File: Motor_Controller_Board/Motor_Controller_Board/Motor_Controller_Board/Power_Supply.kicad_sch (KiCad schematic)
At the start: 11 parts, among them J201 Conn_01x02, J202 Conn_01x02, U201 TP6841S6

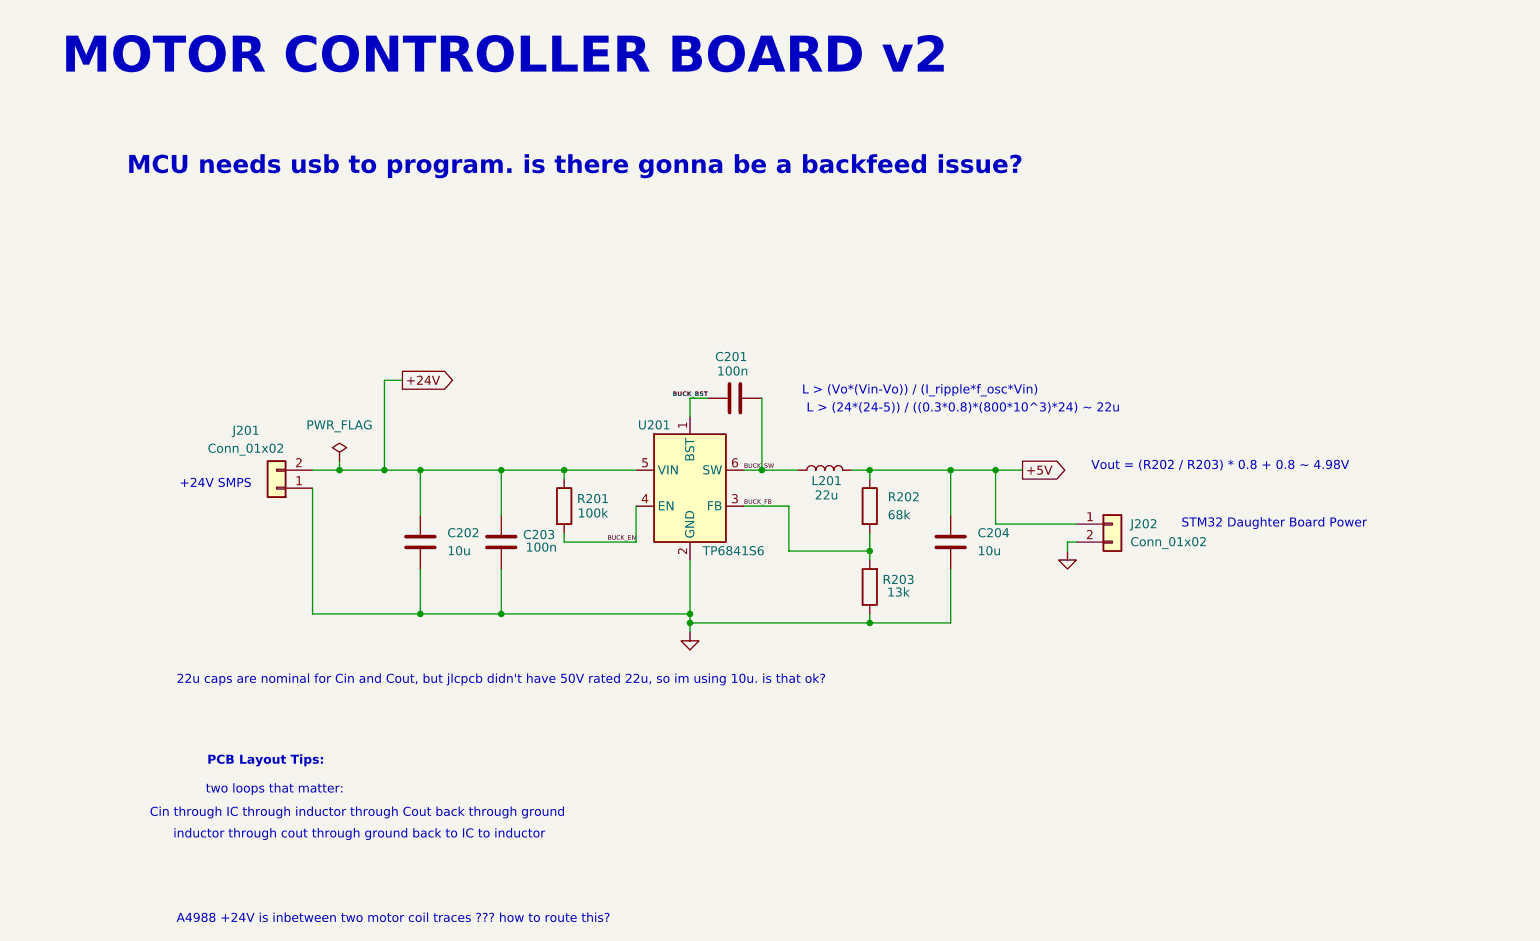
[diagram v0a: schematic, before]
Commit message: discussed with Alex and Mishari. confident in schematic, going to do layout tomorrow
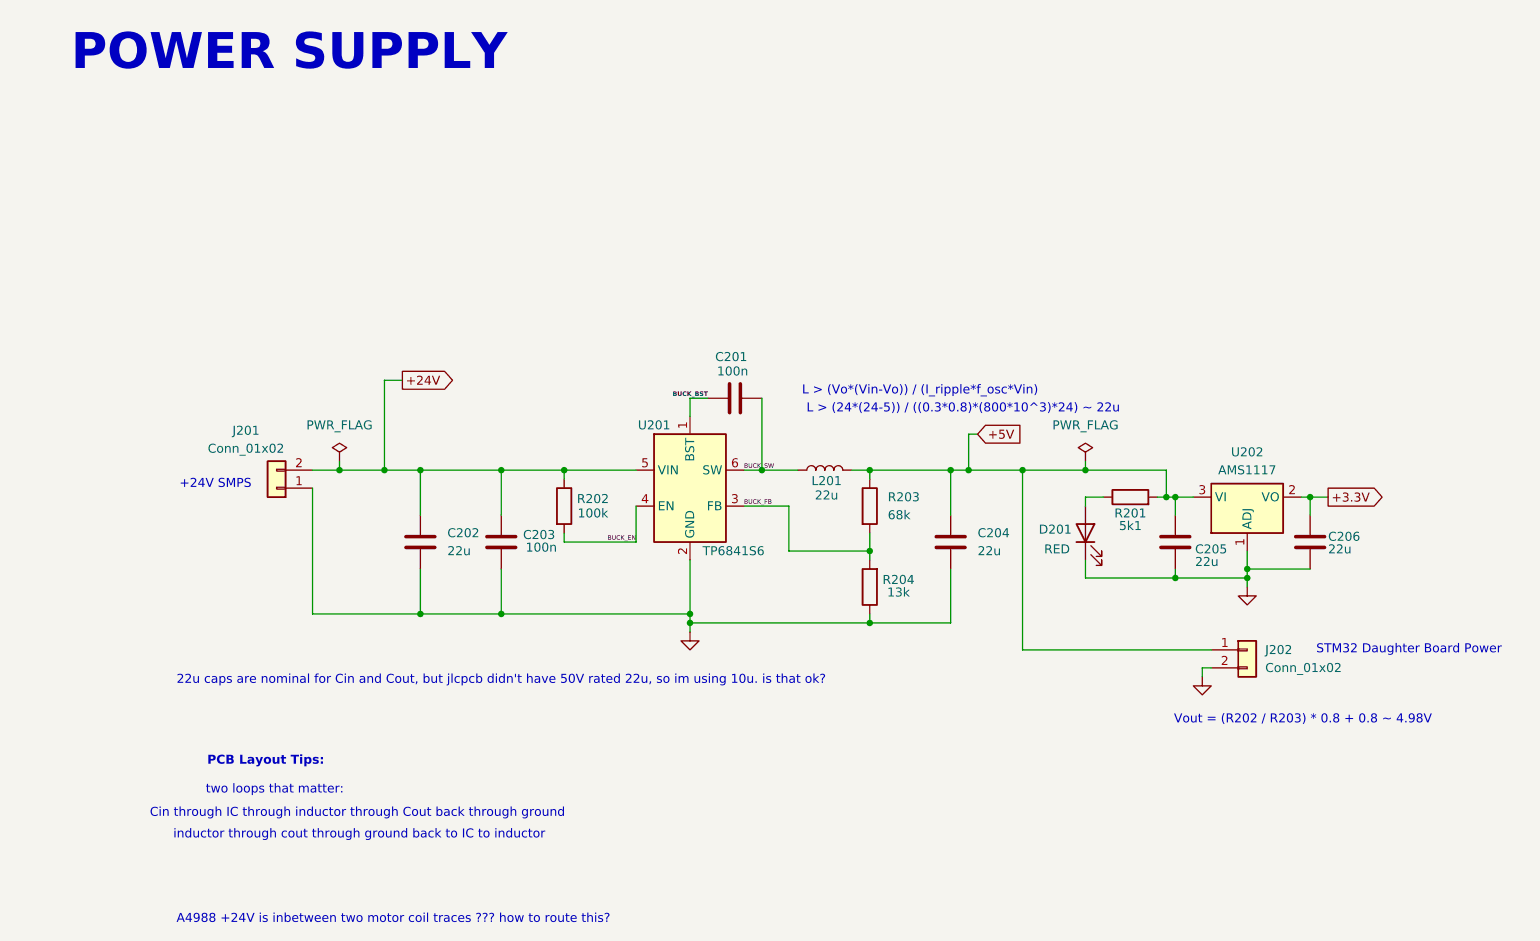
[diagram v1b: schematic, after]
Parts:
- added C205, C206: 22u, Capacitor_SMD:C_0603_1608Metric, symbol Device:C
- added D201: RED, LED_SMD:LED_0603_1608Metric, symbol Device:LED
- added R201: 5k1, Resistor_SMD:R_0603_1608Metric, symbol Device:R
- added U202: AMS1117, Package_TO_SOT_SMD:SOT-223-3_TabPin2, symbol Regulator_Linear:AMS1117
- C202, C204: value 10u -> 22u; footprint Capacitor_SMD:C_0805_2012Metric -> Capacitor_SMD:C_2220_5750Metric; LCSC Part Number C440198 -> C784103; MPN GRM21BR61H106KE43L -> FS55X226K500EHG; Manufacturer Murata Electronics -> PSA(Prosperity Dielectrics)
- J202: now left out of the parts list
- renumbered R201 to R202, R202 to R203, R203 to R204
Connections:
- net +5V: now also C205.1, R201.2, U202.3 (VI)
- net GND: now also C205.2, C206.2, D201.1 (K), U202.1 (ADJ)
- new net: D201.2 (A), R201.1
- new net +3.3V: C206.1, U202.2 (VO)
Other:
- note added: "POWER SUPPLY"
- note removed: "MCU needs usb to program. is there gonna be a backfeed issue?"
- note removed: "MOTOR CONTROLLER BOARD v2"
- moved on the sheet: J202

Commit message: routing 75% finished, but very sloppy
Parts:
- added J203: Conn_01x02, TerminalBlock:TerminalBlock_bornier-2_P5.08mm, symbol Connector_Generic:Conn_01x02
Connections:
- net +24V: now also J203.2 (Pin_2); no longer C202.1, C203.2, J201.2 (Pin_2), R202.1, U201.5 (VIN)
- net GND: now also J203.1 (Pin_1)
- new net DIGITAL_POWER_+24V: C202.1, C203.2, J201.2 (Pin_2), R202.1, U201.5 (VIN)
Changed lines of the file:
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@@
+		)
+	)
+	(text "+24V SMPS"
+		(exclude_from_sim no)
+		(at 32.004 54.102 0)
+		(effects
+			(font
+				(size 1.27 1.27)
+			)
 		)
 	)
@@
 	)
 	(junction
-		(at 55.88 76.2)
-		(diameter 0)
-		(color 0 0 0 0)
-	)
-	(junction
 		(at 167.64 91.44)
 		(diameter 0)
@@
 	(wire
 		(pts
+			(xy 46.99 54.61) (xy 45.72 54.61)
+		)
+		(stroke
+			(width 0)
+			(type default)
+		)
+	)
+	(wire
+		(pts
 			(xy 138.43 71.12) (xy 138.43 76.2)
 		)
@@
 	(wire
 		(pts
+			(xy 46.99 55.88) (xy 46.99 54.61)
+		)
+		(stroke
+			(width 0)
+			(type default)
+		)
+	)
+	(wire
+		(pts
 			(xy 154.94 74.93) (xy 154.94 76.2)
 		)
@@
 	(wire
 		(pts
-			(xy 49.53 76.2) (xy 55.88 76.2)
+			(xy 49.53 76.2) (xy 60.96 76.2)
 		)
 		(stroke
@@
 	(wire
 		(pts
-			(xy 55.88 63.5) (xy 58.42 63.5)
+			(xy 45.72 39.37) (xy 48.26 39.37)
 		)
 		(stroke
@@
 	(wire
 		(pts
-			(xy 55.88 76.2) (xy 55.88 63.5)
+			(xy 45.72 52.07) (xy 45.72 39.37)
 		)
 		(stroke
@@
 		(pts
 			(xy 146.05 101.6) (xy 172.72 101.6)
-		)
-		(stroke
-			(width 0)
-			(type default)
-		)
-	)
-	(wire
-		(pts
-			(xy 55.88 76.2) (xy 60.96 76.2)
 		)
 		(stroke
@@
 			(font
 				(size 0.635 0.635)
+			)
+			(justify left bottom)
+		)
+	)
+	(label "DIGITAL_POWER_+24V"
+		(at 54.61 76.2 0)
+		(effects
+			(font
+				(size 1.27 1.27)
 			)
 			(justify left bottom)
@@
 	(global_label "+24V"
 		(shape output)
-		(at 58.42 63.5 0)
+		(at 48.26 39.37 0)
 		(fields_autoplaced yes)
 		(effects
@@
 		)
 		(property "Intersheetrefs" "${INTERSHEET_REFS}"
-			(at 66.4852 63.5 0)
+			(at 56.3252 39.37 0)
 			(effects
 				(font
@@
 	)
 	(symbol
+		(lib_id "Connector_Generic:Conn_01x02")
+		(at 40.64 54.61 180)
+		(unit 1)
+		(exclude_from_sim no)
+		(in_bom no)
+		(on_board yes)
+		(dnp no)
+		(property "Reference" "J203"
+			(at 36.322 46.482 0)
+			(effects
+				(font
+					(size 1.27 1.27)
+				)
+			)
+		)
+		(property "Value" "Conn_01x02"
+			(at 36.322 49.022 0)
+			(effects
+				(font
+					(size 1.27 1.27)
+				)
+			)
+		)
+		(property "Footprint" "TerminalBlock:TerminalBlock_bornier-2_P5.08mm"
+			(at 40.64 54.61 0)
+			(effects
+				(font
+					(size 1.27 1.27)
+				)
+				(hide yes)
+			)
+		)
+		(property "Datasheet" "~"
+			(at 40.64 54.61 0)
+			(effects
+				(font
+					(size 1.27 1.27)
+				)
+				(hide yes)
+			)
+		)
+		(property "Description" "Generic connector, single row, 01x02, script generated (kicad-library-utils/schlib/autogen/connector/)"
+			(at 40.64 54.61 0)
+			(effects
+				(font
+					(size 1.27 1.27)
+				)
+				(hide yes)
+			)
+		)
+		(pin "1"
+		)
+		(pin "2"
+		)
+		(instances
+			(project "Motor_Controller_Board_v1"
+				(path "/2f03ad95-f17d-4603-9f9b-c868204db81c/1132a342-589f-4523-a20b-cee7da5a1aed"
+					(reference "J203")
+					(unit 1)
+				)
+			)
+		)
+	)
+	(symbol
 		(lib_id "Device:C")
 		(at 72.39 86.36 180)
@@
 					(unit 1)
 				)
+			)
+		)
+	)
+	(symbol
+		(lib_id "power:GND")
+		(at 46.99 55.88 0)
+		(unit 1)
+		(exclude_from_sim no)
+		(in_bom yes)
+		(on_board yes)
+		(dnp no)
+		(fields_autoplaced yes)
+		(property "Reference" "#PWR0205"
+			(at 46.99 62.23 0)
+			(effects
+				(font
+					(size 1.27 1.27)
+				)
+				(hide yes)
+			)
+		)
+		(property "Value" "GND"
+			(at 46.99 60.96 0)
+			(effects
+				(font
+					(size 1.27 1.27)
+				)
+				(hide yes)
+			)
+		)
+		(property "Footprint" ""
+			(at 46.99 55.88 0)
+			(effects
+				(font
+					(size 1.27 1.27)
+				)
+				(hide yes)
+			)
+		)
+		(property "Datasheet" ""
+			(at 46.99 55.88 0)
+			(effects
+				(font
+					(size 1.27 1.27)
+				)
+				(hide yes)
+			)
+		)
+		(property "Description" "Power symbol creates a global label with name \"GND\" , ground"
+			(at 46.99 55.88 0)
+			(effects
+				(font
+					(size 1.27 1.27)
+				)
+				(hide yes)
+			)
+		)
+		(pin "1"
+		)
+		(instances
+			(project "Motor_Controller_Board_v1"
+				(path "/2f03ad95-f17d-4603-9f9b-c868204db81c/1132a342-589f-4523-a20b-cee7da5a1aed"
+					(reference "#PWR0205")
+					(unit 1)
+				)
